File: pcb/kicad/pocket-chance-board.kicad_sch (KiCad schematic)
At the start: 137 parts, among them J1 SWD, J2 USB4085-GF-A, J3 LiPo JST-PH 2.0mm (1 = + RED,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, J4 LCD 1.54in ST7789 module, JST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, J5 Speaker JST-PH, J6 microSD Molex 104031-0811, J7 STEMMA QT, J8 Expansion (6 = VBAT_SENSE ADC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, Q1 FS8205A, Q2 AO3401A, Q3 AO3400A, Q4 AO3401A, Q5 AO3400A, SW1 BOOT, SW10 DPAD LEFT PTS645SM43SMTR92, SW11 DPAD RIGHT PTS645SM43SMTR92, SW12 DPAD PRESS PTS645SM43SMTR92, SW2 RESET, SW3 POWER PCM12, SW4 A PTS125SM43SMTR2LFS, SW5 B PTS125SM43SMTR2LFS, SW6 X PTS125SM43SMTR2LFS, SW7 Y PTS125SM43SMTR2LFS, SW8 DPAD UP PTS645SM43SMTR92, SW9 DPAD DOWN PTS645SM43SMTR92, U1 RP2350A, U10 LSM6DSOXTR, U11 RM2, U2 W25Q128JVSIQ, U3 APS6404L-3SQR-SN, U4 USBLC6-2SC6, U5 BQ24074RGTR, U6 TPS63001DRCR, U7 DW01A, U8 PAM8302AADCR, U9 DS3231MZ+, Y1 12MHz ABM8-272-T3

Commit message: Rev 0.6: electronic reverse-polarity guard removed (John, option B after AUDIT-3); procedural protection recorded on the sheet and in the documents
Co-Authored-By: Claude Fable 5.1 <noreply@anthropic.com>
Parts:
- removed Q2: AO3401A, Package_TO_SOT_SMD:SOT-23, symbol Transistor_FET:AO3401A
- removed Q5: AO3400A, Package_TO_SOT_SMD:SOT-23, symbol Transistor_FET:AO3400A
- removed R45: 100k, Resistor_SMD:R_0402_1005Metric, symbol Device:R
- removed R46: 10k, Resistor_SMD:R_0402_1005Metric, symbol Device:R
- removed R47: 47k, Resistor_SMD:R_0402_1005Metric, symbol Device:R
- removed R48: 1M, Resistor_SMD:R_0402_1005Metric, symbol Device:R
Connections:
- net CELL_G is gone; now on net CELL_P: R22.1
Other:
- note added: "BATTERY (PCB-001, owner decisions 2026-10-04): one protected LiPo pouch cell, 1000 mAh or more, rated 0.5 C charge, charging 0 to 45 C, JST-PH plug, + on pin 1 = RED WIRE, pin 3 = cell thermistor (remove R12 if used). Charge current 494 mA (R14 1.8k; 3.6k for 500 mAh). NO ON-BOARD REVERSE-POLARITY GUARD (rev 0.6, as on the Pico W): the keyed plug, the silkscreen, one approved cell listing and che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"
- note removed: "BATTERY (PCB-001, owner decision 2026-10-04): one protected LiPo pouch cell, 1000 mAh or more, rated 0.5 C charge, charge temperature 0 to 45 C, JST-PH plug, + on pin 1 (red wire). Charge current 494 mA (R14 1.8k; 3.6k for 500 mAh). The charger does NOT sense the cell's temperature with a two-wire cell (R12 10k fitted = check bypassed); it relies on the cell's own protection board and the 0.5 C r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"

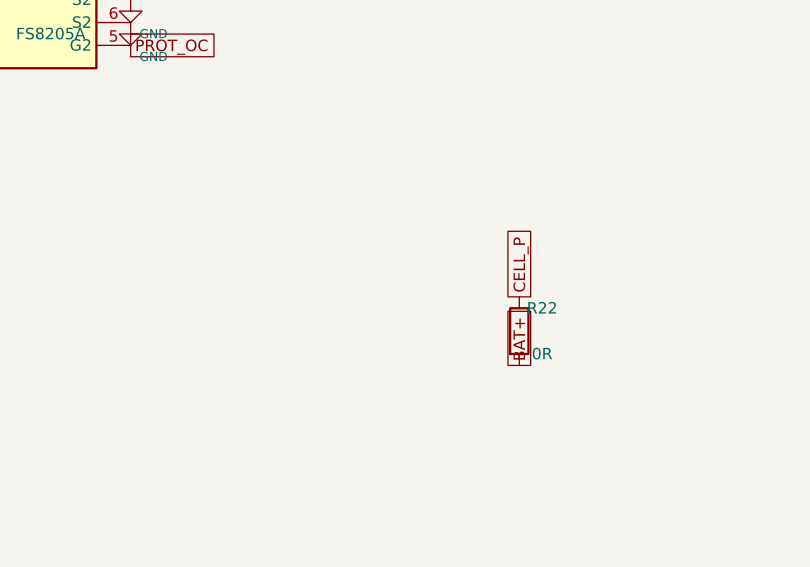
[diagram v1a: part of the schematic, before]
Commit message: Rev 0.7: F1 polyfuse (MF-MSMF110/16X-2, 1.1 A hold) in the cell lead (John, option D); R20 to 0603
Co-Authored-By: Claude Fable 5.1 <noreply@anthropic.com>
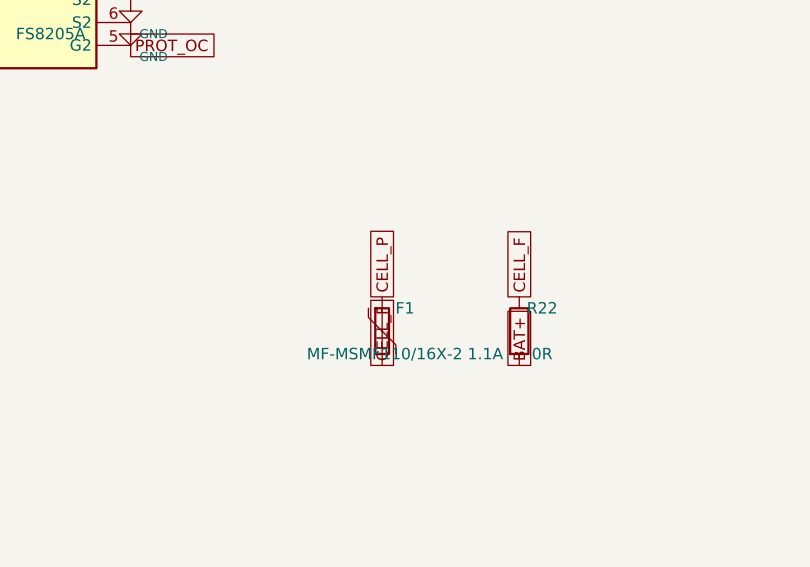
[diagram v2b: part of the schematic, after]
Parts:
- added F1: MF-MSMF110/16X-2 1.1A, Fuse:Fuse_1812_4532Metric, symbol Device:Polyfuse
- R20: footprint Resistor_SMD:R_0402_1005Metric -> Resistor_SMD:R_0603_1608Metric
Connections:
- net CELL_P: now also F1.1; no longer R22.1
- new net CELL_F: F1.2, R22.1
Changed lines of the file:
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@@
 		(title "Pocket Chance board, spin 1")
 		(date "2026-10-04")
-		(rev "0.6")
+		(rev "0.7")
 		(company "Pocket Chance")
 		(comment 1 "Generated by pcb/tools/gen_sch.py from the connection table. Label-based: every pin carries its net name.")
@@
 			)
 		)
-		(property "Footprint" "Resistor_SMD:R_0402_1005Metric"
+		(property "Footprint" "Resistor_SMD:R_0603_1608Metric"
 			(at 340.36 335.28 0)
 			(effects
@@
 	)
 	(symbol
+		(lib_id "Device:Polyfuse")
+		(at 379.73 400.05 0)
+		(unit 1)
+		(exclude_from_sim no)
+		(in_bom yes)
+		(on_board yes)
+		(dnp no)
+		(property "Reference" "F1"
+			(at 382.27 397.51 0)
+			(effects
+				(font
+					(size 1.27 1.27)
+				)
+			)
+		)
+		(property "Value" "MF-MSMF110/16X-2 1.1A"
+			(at 382.27 402.59 0)
+			(effects
+				(font
+					(size 1.27 1.27)
+				)
+			)
+		)
+		(property "Footprint" "Fuse:Fuse_1812_4532Metric"
+			(at 379.73 400.05 0)
+			(effects
+				(font
+					(size 1.27 1.27)
+				)
+				hide
+			)
+		)
+		(property "Datasheet" ""
+			(at 379.73 400.05 0)
+			(effects
+				(font
+					(size 1.27 1.27)
+				)
+				hide
+			)
+		)
+		(pin "1"
+		)
+		(pin "2"
+		)
+		(instances
+			(project "pocket-chance-board"
+				(path "/4a96f16e-da4b-424f-949b-4389eda2fe0f"
+					(reference "F1")
+					(unit 1)
+				)
+			)
+		)
+	)
+	(global_label "CELL_P"
+		(shape passive)
+		(at 379.73 396.24 90)
+		(fields_autoplaced yes)
+		(effects
+			(font
+				(size 1.27 1.27)
+			)
+			(justify left)
+		)
+		(property "Intersheetrefs" "${INTERSHEET_REFS}"
+			(at 379.73 396.24 0)
+			(effects
+				(font
+					(size 1.27 1.27)
+				)
+				hide
+			)
+		)
+	)
+	(global_label "CELL_F"
+		(shape passive)
+		(at 379.73 403.86 270)
+		(fields_autoplaced yes)
+		(effects
+			(font
+				(size 1.27 1.27)
+			)
+			(justify left)
+		)
+		(property "Intersheetrefs" "${INTERSHEET_REFS}"
+			(at 379.73 403.86 0)
+			(effects
+				(font
+					(size 1.27 1.27)
+				)
+				hide
+			)
+		)
+	)
+	(symbol
 		(lib_id "Device:R")
 		(at 394.97 400.05 0)
@@
 		)
 	)
-	(global_label "CELL_P"
+	(global_label "CELL_F"
 		(shape passive)
 		(at 394.97 396.24 90)

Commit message: AUDIT-3 rev 0.6 instructions: sheet note wrapped (PDF clipping), timer and 274 mA wording, USB4085 is hybrid through-hole, screen rows corrected (no price saving, sizing, generic order, Adafruit 4313)
Co-Authored-By: Claude Fable 5.1 <noreply@anthropic.com>
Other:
- note added: "BATTERY (PCB-001, owner decisions 2026-10-04) - One protected LiPo pouch cell, 1000 mAh or more, rated 0.5 C charge, charging 0 to 45 C, JST-PH plug, + on pin 1 = RED WIRE, pin 3 = cell thermistor (remove R12 if used). Charge current 494 mA (R14 1.8k; 3.6k for 500 mAh, up to 274 mA at tolerance). - NO ON-BOARD REVERSE-POLARITY GUARD (rev 0.6, as on the Pico W). F1 polyfuse in the cell lead (rev 0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"
- note removed: "BATTERY (PCB-001, owner decisions 2026-10-04): one protected LiPo pouch cell, 1000 mAh or more, rated 0.5 C charge, charging 0 to 45 C, JST-PH plug, + on pin 1 = RED WIRE, pin 3 = cell thermistor (remove R12 if used). Charge current 494 mA (R14 1.8k; 3.6k for 500 mAh). NO ON-BOARD REVERSE-POLARITY GUARD (rev 0.6, as on the Pico W): the keyed plug, the silkscreen, one approved cell listing and che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"
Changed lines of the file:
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@@
 		)
 	)
-	(text "BATTERY (PCB-001, owner decisions 2026-10-04): one protected LiPo pouch cell, 1000 mAh or more, rated 0.5 C charge, charging 0 to 45 C, JST-PH plug, + on pin 1 = RED WIRE, pin 3 = cell thermistor (remove R12 if used). Charge current 494 mA (R14 1.8k; 3.6k for 500 mAh). NO ON-BOARD REVERSE-POLARITY GUARD (rev 0.6, as on the Pico W): the keyed plug, the silkscreen, one approved cell listing and checking the wire colours BEFORE plugging in are the protection; a mis-wired cell can damage the DW01A and the charger's BAT pin (-0.3 V limits). UNPLUG USB BEFORE SWAPPING CELLS. The charger does not sense the cell's temperature with a two-wire cell (R12 10k fitted = check bypassed): the cell's protection board and the 0.5 C rate protect it. First power-ups: current-limited supply, no cell; then cell alone with the meter; then both. Charge on a non-flammable surface, never unattended."
+	(text "BATTERY (PCB-001, owner decisions 2026-10-04)
+- One protected LiPo pouch cell, 1000 mAh or more, rated 0.5 C charge, charging 0 to 45 C, JST-PH plug, + on pin 1 = RED WIRE,
+  pin 3 = cell thermistor (remove R12 if used). Charge current 494 mA (R14 1.8k; 3.6k for 500 mAh, up to 274 mA at tolerance).
+- NO ON-BOARD REVERSE-POLARITY GUARD (rev 0.6, as on the Pico W). F1 polyfuse in the cell lead (rev 0.7) contains shorts and
+  limits heat after a wiring mistake but does NOT save the two chips a reversed cell destroys. The keyed plug, the silkscreen,
+  one approved cell listing and checking the wire colours BEFORE plugging in are the protection; a mis-wired cell can damage
+  the DW01A and the charger's BAT pin (-0.3 V limits). UNPLUG USB BEFORE SWAPPING CELLS (the socket is live from the charger).
+- The charger does not sense the cell's temperature with a two-wire cell (R12 10k fitted = check bypassed): the cell's
+  protection board and the 0.5 C rate protect it. Safety timer about 6 h, longer while the charger throttles (DPPM, thermal).
+- First power-ups: current-limited supply, no cell; then cell alone with the meter; then both. Charge on a non-flammable
+  surface, never unattended. A tripped F1 resets only after the cell is unplugged."
 		(exclude_from_sim no)
 		(at 290 470 0)
